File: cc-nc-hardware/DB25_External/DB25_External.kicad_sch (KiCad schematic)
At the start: 85 parts, among them J1 Conn_01x03_Male, J2 DB25_Male_MountingHoles, J4 SW, J6 Conn_01x02_Male, SW1 SW_MEC_5E, U1 SN74CBTD3384, U2 SN74CBTD3384, U3 AMS1117-2.85, U4 LVT245, U5 LVT125, U6 LVT125, U7 LVT125, U9 LVT245

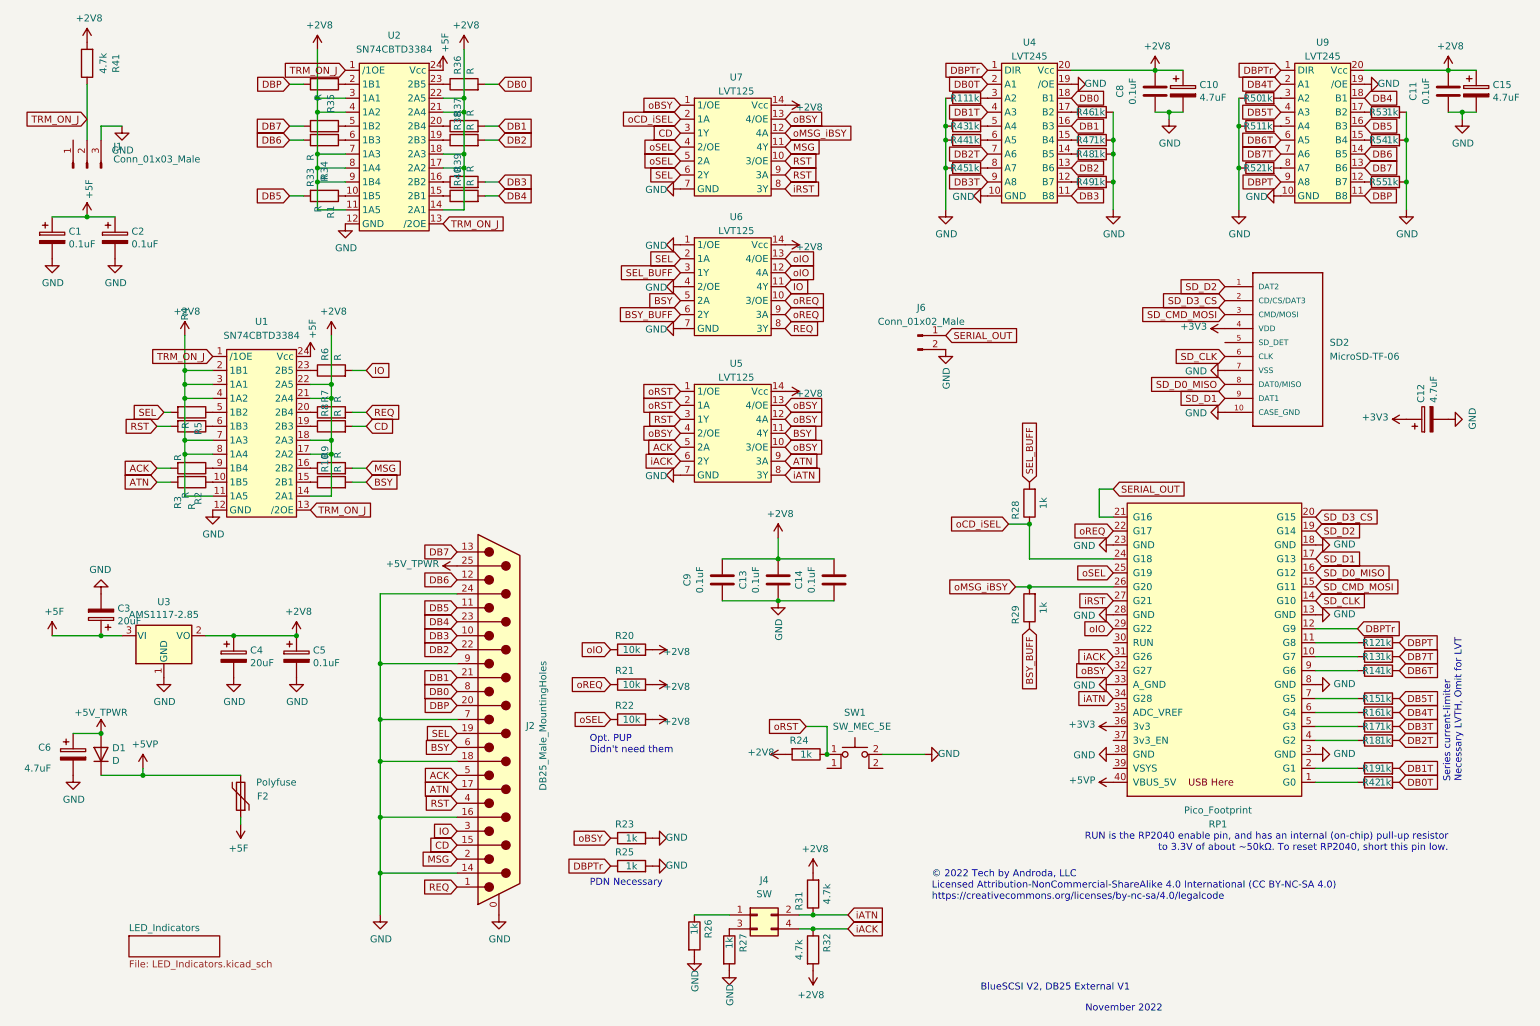
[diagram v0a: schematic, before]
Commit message: DB25 2023_06a, Smaller Design
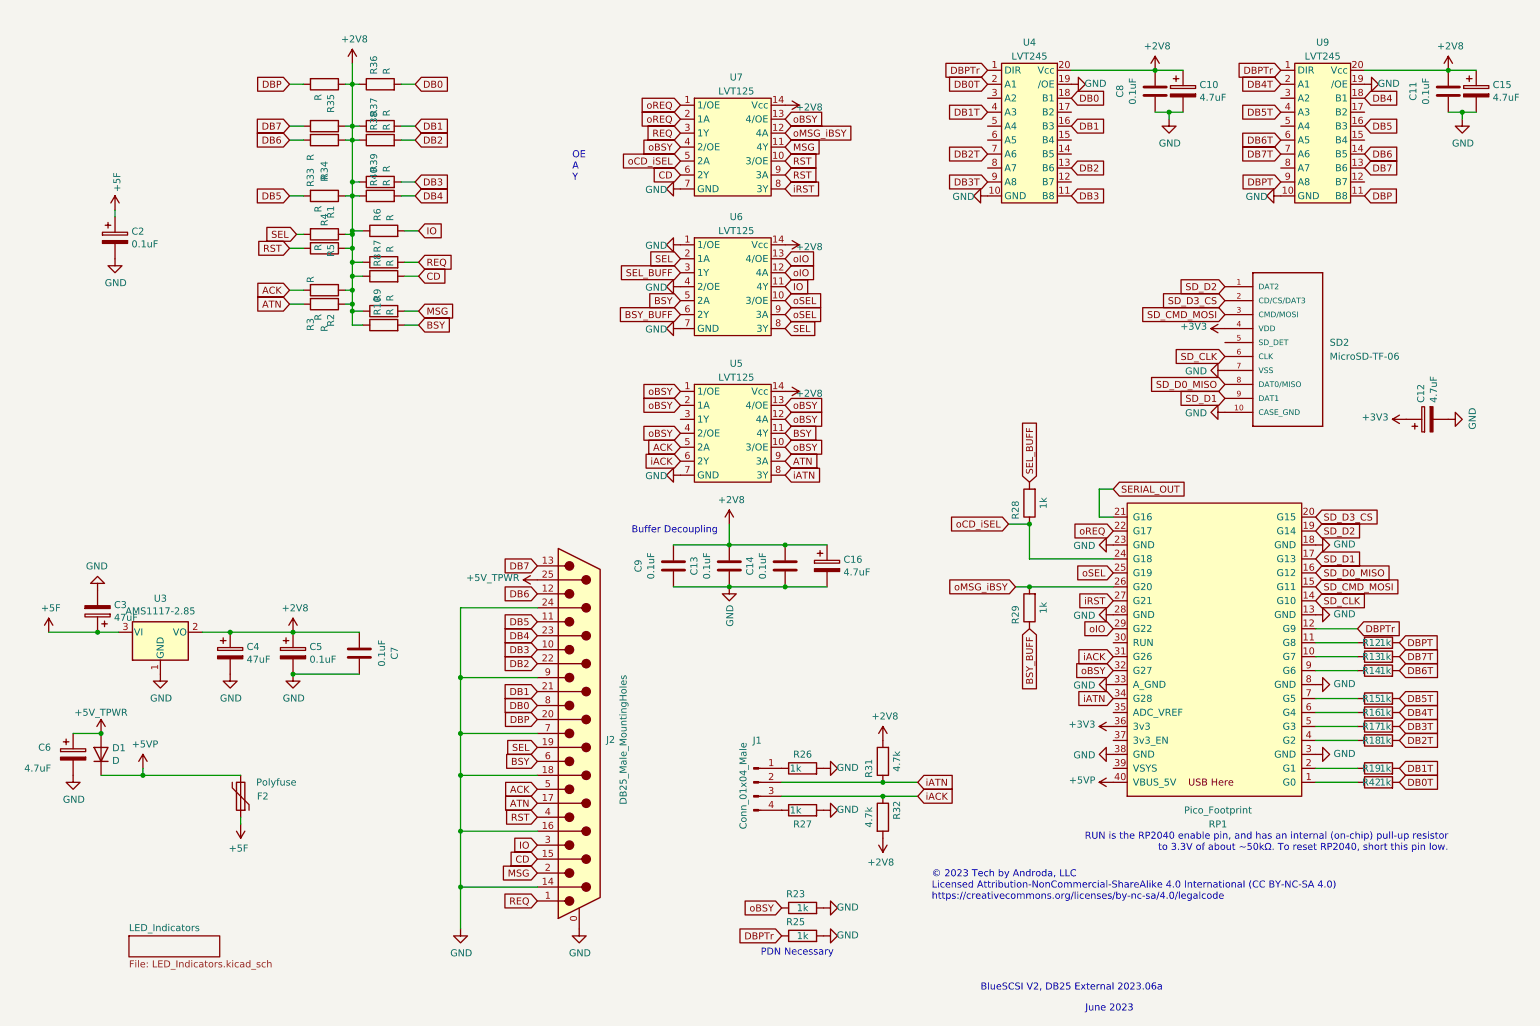
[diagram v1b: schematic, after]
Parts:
- removed C1: 0.1uF, Capacitor_SMD:C_0805_2012Metric_Pad1.15x1.40mm_HandSolder, symbol Device:CP
- removed J1: Conn_01x03_Male, Connector_PinHeader_2.54mm:PinHeader_1x03_P2.54mm_Vertical, symbol Connector:Conn_01x03_Male
- removed J4: SW, Connector_PinHeader_2.54mm:PinHeader_2x02_P2.54mm_Vertical, symbol Connector_Generic:Conn_02x02_Odd_Even
- removed J6: Conn_01x02_Male, Connector_PinHeader_2.54mm:PinHeader_1x02_P2.54mm_Vertical, symbol Connector:Conn_01x02_Male
- removed R11, R43, R44, R45, R46, R47, R48, R49, R50, R51, R52, R53, R54, R55: 1k, Resistor_SMD:R_0402_1005Metric_Pad0.72x0.64mm_HandSolder, symbol Device:R
- removed R20, R21, R22: 10k, Resistor_SMD:R_0603_1608Metric_Pad0.98x0.95mm_HandSolder, symbol Device:R
- removed R24: 1k, Resistor_SMD:R_0603_1608Metric_Pad0.98x0.95mm_HandSolder, symbol Device:R
- removed R41: 4.7k, Resistor_SMD:R_0603_1608Metric_Pad0.98x0.95mm_HandSolder, symbol Device:R
- removed SW1: SW_MEC_5E, Library:TS-1187A-B-A-B, symbol Switch:SW_MEC_5E
- removed U1, U2: SN74CBTD3384, Package_SO:TSSOP-24_4.4x7.8mm_P0.65mm, symbol New_Library:SN74CBTD3384
- added C16: 4.7uF, Capacitor_SMD:C_0805_2012Metric_Pad1.18x1.45mm_HandSolder, symbol Device:CP
- added C7: 0.1uF, Capacitor_SMD:C_0603_1608Metric_Pad1.08x0.95mm_HandSolder, symbol Device:C
- added J1: Conn_01x04_Male, Connector_PinHeader_2.54mm:PinHeader_1x04_P2.54mm_Vertical, symbol Connector:Conn_01x04_Male
- C13, C14, C9: footprint Capacitor_SMD:C_0805_2012Metric_Pad1.18x1.45mm_HandSolder -> Capacitor_SMD:C_0603_1608Metric_Pad1.08x0.95mm_HandSolder
- C3, C4: value 20uF -> 47uF
- R12, R13, R14, R15, R16, R17, R18, R19, R42: footprint Resistor_SMD:R_0402_1005Metric_Pad0.72x0.64mm_HandSolder -> Resistor_SMD:R_0603_1608Metric_Pad0.98x0.95mm_HandSolder
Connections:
- net oRST is gone; now on net oBSY: U5.1 (1/OE), U5.2 (1A)
- net +2V8: now also R1.1, R10.1, R2.1, R3.1, R33.1, R34.1, R35.1, R36.1, R37.1, R38.1, R39.1, R4.1, R40.1, R5.1, R6.1, R7.1, R8.1, R9.1, C16.1, C7.1
- net CD: now also U7.6 (2Y); no longer U7.3 (1Y)
- net GND: now also C16.2, C7.2
- net REQ: now also U7.3 (1Y); no longer U6.8 (3Y)
- net RST: no longer U5.3 (1Y)
- net SEL: now also U6.8 (3Y); no longer U7.6 (2Y)
- net iACK: now also J1.3 (Pin_3)
- net iATN: now also J1.2 (Pin_2)
- net oBSY: now also U7.4 (2/OE); no longer U7.1 (1/OE)
- net oCD_iSEL: now also U7.5 (2A); no longer U7.2 (1A)
- net oREQ: now also U7.1 (1/OE), U7.2 (1A); no longer U6.10 (3/OE), U6.9 (3A)
- net oSEL: now also U6.10 (3/OE), U6.9 (3A); no longer U7.4 (2/OE), U7.5 (2A)
- net at R26.1: now also J1.1 (Pin_1)
- net at R27.1: now also J1.4 (Pin_4)
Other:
- note added: "BlueSCSI V2, DB25 External 2023.06a"
- note added: "Buffer Decoupling"
- note added: "June 2023"
- note added: "OE A Y"
- note added: "© 2023 Tech by Androda, LLC Licensed Attribution-NonCommercial-ShareAlike 4.0 International (CC BY-NC-SA 4.0) https://creativecommons.org/licenses/by-nc-sa/4.0/legalcode"
- note removed: "BlueSCSI V2, DB25 External V1"
- note removed: "November 2022"
- note removed: "Opt. PUP Didn't need them"
- note removed: "Series current-limiter Necessary LVTH, Omit for LVT"
- note removed: "© 2022 Tech by Androda, LLC Licensed Attribution-NonCommercial-ShareAlike 4.0 International (CC BY-NC-SA 4.0) https://creativecommons.org/licenses/by-nc-sa/4.0/legalcode"
- moved on the sheet: C13, C14, C3, C4, C5, C9, J2, R10, R2, R23, R25, R26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

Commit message: Update DB25 schematic for greater clarity
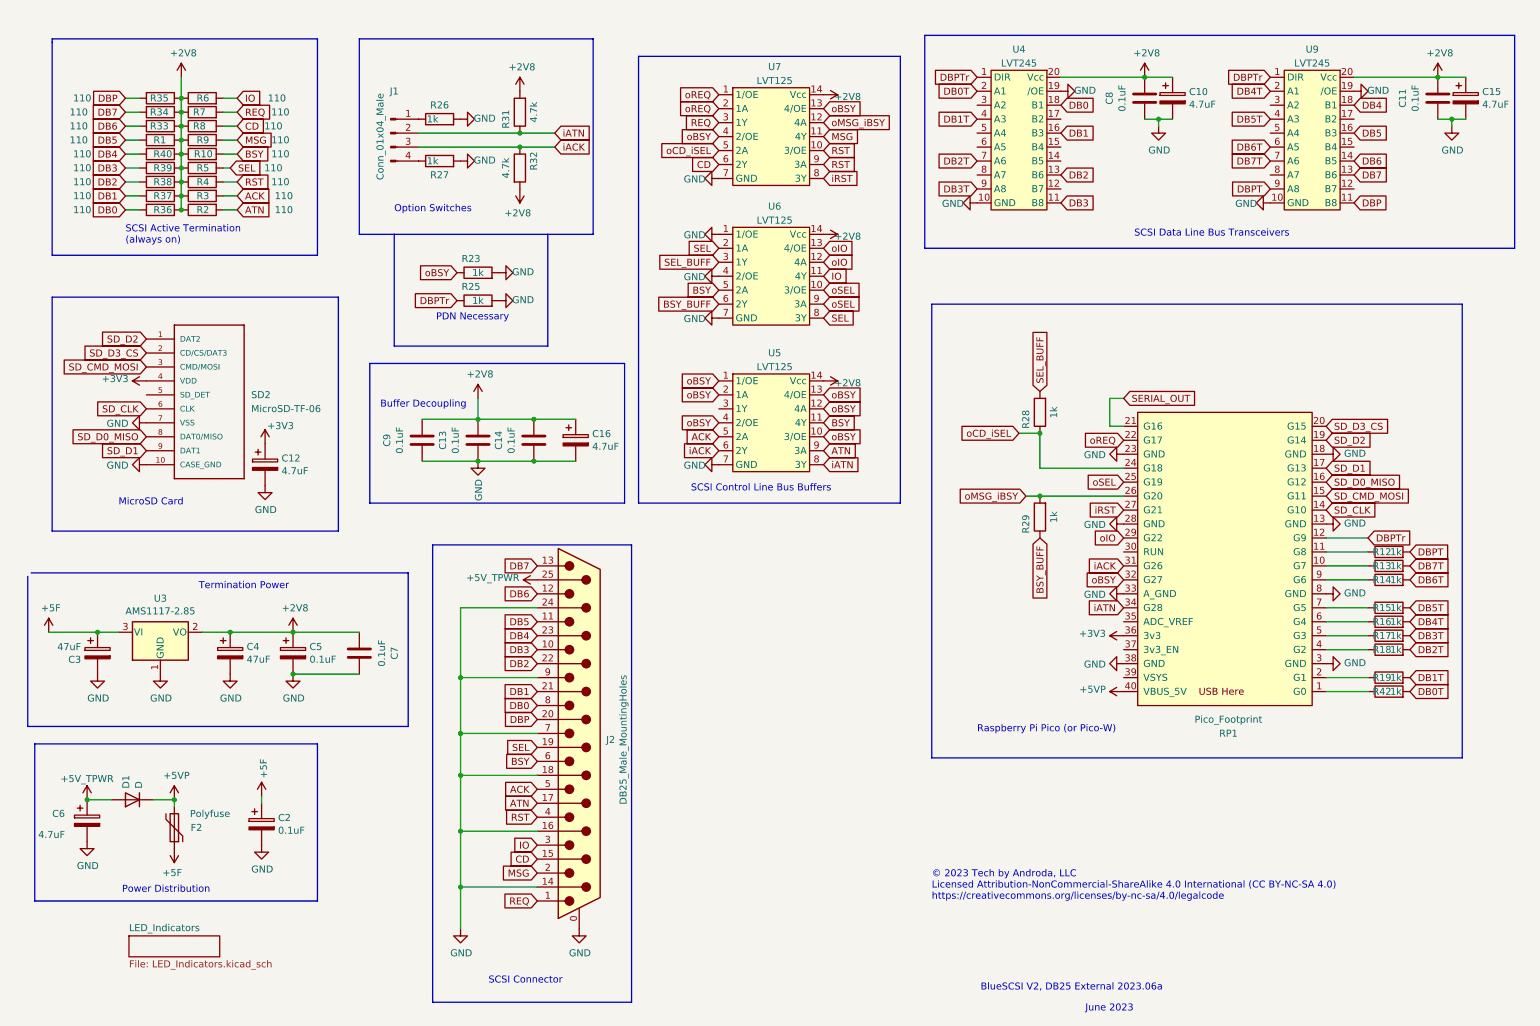
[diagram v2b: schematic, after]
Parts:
- R1, R10, R2, R3, R33, R34, R35, R36, R37, R38, R39, R4, R40, R5, R6, R7, R8, R9: value R -> 110
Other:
- note added: "MicroSD Card"
- note added: "Option Switches"
- note added: "Power Distribution"
- note added: "Raspberry Pi Pico (or Pico-W)"
- note added: "SCSI Active Termination (always on)"
- note added: "SCSI Connector"
- note added: "SCSI Control Line Bus Buffers"
- note added: "SCSI Data Line Bus Transceivers"
- note added: "Termination Power"
- note removed: "OE A Y"
- note removed: "RUN is the RP2040 enable pin, and has an internal (on-chip) pull-up resistor to 3.3V of about ~50kΩ. To reset RP2040, short this pin low."
- moved on the sheet: C10, C11, C12, C13, C14, C15, C16, C2, C3, C6, C8, C9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

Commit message: DB25 Hardware Version 2024.01a, Narrower
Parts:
- removed J1: Conn_01x04_Male, Connector_PinHeader_2.54mm:PinHeader_1x04_P2.54mm_Vertical, symbol Connector:Conn_01x04_Male
- removed R27: 1k, Resistor_SMD:R_0603_1608Metric_Pad0.98x0.95mm_HandSolder, symbol Device:R
- removed R31, R32: 4.7k, Resistor_SMD:R_0603_1608Metric_Pad0.98x0.95mm_HandSolder, symbol Device:R
- removed R36, R37, R38, R39, R40: 110, Resistor_SMD:R_0603_1608Metric_Pad0.98x0.95mm_HandSolder, symbol Device:R
- added R20, R21, R22, R24: 110, Resistor_SMD:R_0603_1608Metric_Pad0.98x0.95mm_HandSolder, symbol Device:R
- R26: value 1k -> 110
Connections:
- net +2V8: now also R26.1, R20.1, R21.1, R22.1, R24.1
- net DB0: now also R20.2
- net DB1: now also R21.2
- net DB2: now also R22.2
- net DB3: now also R24.2
- net DB4: now also R26.2
- net GND: no longer R26.2
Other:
- note added: "BlueSCSI V2, DB25 External 2024.01a"
- note added: "January 2024"
- note added: "© 2023 - 2024 Tech by Androda, LLC Licensed Attribution-NonCommercial-ShareAlike 4.0 International (CC BY-NC-SA 4.0) https://creativecommons.org/licenses/by-nc-sa/4.0/legalcode"
- note removed: "BlueSCSI V2, DB25 External 2023.06a"
- note removed: "June 2023"
- note removed: "Option Switches"
- note removed: "© 2023 Tech by Androda, LLC Licensed Attribution-NonCommercial-ShareAlike 4.0 International (CC BY-NC-SA 4.0) https://creativecommons.org/licenses/by-nc-sa/4.0/legalcode"
- moved on the sheet: C10, C11, C12, C13, C14, C15, C16, C2, C3, C4, C5, C6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
